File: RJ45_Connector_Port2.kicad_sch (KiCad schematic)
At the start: 8 parts, among them J1 0826-1X4T-43-F

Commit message: Adding page title, and confidential for now
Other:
- title: (none) -> RJ45 Connector Port 2
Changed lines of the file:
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@@
 	(paper "A4")
 	(title_block
+		(title "RJ45 Connector Port 2")
 		(date "2025-12-21")
 		(rev "Rev. A")
 		(company "Kebag-Logic <contact@kebag-logic.com>")
+		(comment 1 "Confidential")
 	)
 	(junction

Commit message: fixes ERC errors in DC/DC converters
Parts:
- C11, C12, C13, C14: footprint Capacitor_SMD:C_0201_0603Metric -> KL_Footprints:C_0603; Dielectric X7R -> (none); Farnell 4539043 -> (none); Package_in_inch 0603 -> (none); Tolerance_in_pct 10 -> (none)
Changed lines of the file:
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@@
 		(dnp no)
 		(property "Reference" "C13"
-			(at 80.01 58.674 90)
-			(effects
-				(font
-					(size 1.27 1.27)
-				)
+			(at 77.47 61.595 0)
+			(effects
+				(font
+					(size 1.27 1.27)
+				)
+				(justify left)
 			)
 		)
 		(property "Value" "100n"
-			(at 80.01 65.532 90)
-			(effects
-				(font
-					(size 1.27 1.27)
-				)
-			)
-		)
-		(property "Footprint" "Capacitor_SMD:C_0201_0603Metric"
+			(at 82.55 61.595 0)
+			(effects
+				(font
+					(size 1.27 1.27)
+				)
+				(justify left)
+			)
+		)
+		(property "Footprint" "KL_Footprints:C_0603"
 			(at 83.82 61.2648 0)
 			(effects
@@
 		)
 		(property "LCSC" "C1591"
-			(at 80.01 62.23 0)
-			(effects
-				(font
-					(size 1.27 1.27)
-				)
-				(hide yes)
-			)
-		)
-		(property "Tolerance_in_pct" "10"
-			(at 80.01 62.23 0)
-			(effects
-				(font
-					(size 1.27 1.27)
-				)
-				(hide yes)
-			)
-		)
-		(property "Dielectric" "X7R"
-			(at 80.01 62.23 0)
-			(effects
-				(font
-					(size 1.27 1.27)
-				)
-				(hide yes)
-			)
-		)
-		(property "Package_in_inch" "0603"
-			(at 80.01 62.23 0)
-			(effects
-				(font
-					(size 1.27 1.27)
-				)
-				(hide yes)
-			)
-		)
-		(property "Farnell" "4539043"
 			(at 80.01 62.23 0)
 			(effects
@@
 		(dnp no)
 		(property "Reference" "C11"
-			(at 80.01 38.354 90)
-			(effects
-				(font
-					(size 1.27 1.27)
-				)
+			(at 82.55 42.545 0)
+			(effects
+				(font
+					(size 1.27 1.27)
+				)
+				(justify left)
 			)
 		)
 		(property "Value" "100n"
-			(at 80.01 45.212 90)
-			(effects
-				(font
-					(size 1.27 1.27)
-				)
-			)
-		)
-		(property "Footprint" "Capacitor_SMD:C_0201_0603Metric"
+			(at 77.47 42.545 0)
+			(effects
+				(font
+					(size 1.27 1.27)
+				)
+				(justify left)
+			)
+		)
+		(property "Footprint" "KL_Footprints:C_0603"
 			(at 76.2 42.8752 0)
 			(effects
@@
 		)
 		(property "LCSC" "C1591"
-			(at 80.01 41.91 0)
-			(effects
-				(font
-					(size 1.27 1.27)
-				)
-				(hide yes)
-			)
-		)
-		(property "Tolerance_in_pct" "10"
-			(at 80.01 41.91 0)
-			(effects
-				(font
-					(size 1.27 1.27)
-				)
-				(hide yes)
-			)
-		)
-		(property "Dielectric" "X7R"
-			(at 80.01 41.91 0)
-			(effects
-				(font
-					(size 1.27 1.27)
-				)
-				(hide yes)
-			)
-		)
-		(property "Package_in_inch" "0603"
-			(at 80.01 41.91 0)
-			(effects
-				(font
-					(size 1.27 1.27)
-				)
-				(hide yes)
-			)
-		)
-		(property "Farnell" "4539043"
 			(at 80.01 41.91 0)
 			(effects
@@
 		(dnp no)
 		(property "Reference" "C12"
-			(at 80.01 48.768 90)
-			(effects
-				(font
-					(size 1.27 1.27)
-				)
+			(at 77.47 51.435 0)
+			(effects
+				(font
+					(size 1.27 1.27)
+				)
+				(justify left)
 			)
 		)
 		(property "Value" "100n"
-			(at 80.01 55.372 90)
-			(effects
-				(font
-					(size 1.27 1.27)
-				)
-			)
-		)
-		(property "Footprint" "Capacitor_SMD:C_0201_0603Metric"
+			(at 82.55 51.435 0)
+			(effects
+				(font
+					(size 1.27 1.27)
+				)
+				(justify left)
+			)
+		)
+		(property "Footprint" "KL_Footprints:C_0603"
 			(at 83.82 51.1048 0)
 			(effects
@@
 		)
 		(property "LCSC" "C1591"
-			(at 80.01 52.07 0)
-			(effects
-				(font
-					(size 1.27 1.27)
-				)
-				(hide yes)
-			)
-		)
-		(property "Tolerance_in_pct" "10"
-			(at 80.01 52.07 0)
-			(effects
-				(font
-					(size 1.27 1.27)
-				)
-				(hide yes)
-			)
-		)
-		(property "Dielectric" "X7R"
-			(at 80.01 52.07 0)
-			(effects
-				(font
-					(size 1.27 1.27)
-				)
-				(hide yes)
-			)
-		)
-		(property "Package_in_inch" "0603"
-			(at 80.01 52.07 0)
-			(effects
-				(font
-					(size 1.27 1.27)
-				)
-				(hide yes)
-			)
-		)
-		(property "Farnell" "4539043"
 			(at 80.01 52.07 0)
 			(effects
@@
 		(dnp no)
 		(property "Reference" "C14"
-			(at 80.01 68.834 90)
-			(effects
-				(font
-					(size 1.27 1.27)
-				)
+			(at 77.47 71.755 0)
+			(effects
+				(font
+					(size 1.27 1.27)
+				)
+				(justify left)
 			)
 		)
 		(property "Value" "100n"
-			(at 80.01 75.946 90)
-			(effects
-				(font
-					(size 1.27 1.27)
-				)
-			)
-		)
-		(property "Footprint" "Capacitor_SMD:C_0201_0603Metric"
+			(at 82.55 71.755 0)
+			(effects
+				(font
+					(size 1.27 1.27)
+				)
+				(justify left)
+			)
+		)
+		(property "Footprint" "KL_Footprints:C_0603"
 			(at 83.82 71.4248 0)
 			(effects
@@
 			(at 80.01 72.39 0)
 			(effects
-				(font
-					(size 1.27 1.27)
-				)
-				(hide yes)
-			)
-		)
-		(property "Tolerance_in_pct" "10"
-			(at 80.01 72.39 0)
-			(effects
-				(font
-					(size 1.27 1.27)
-				)
-				(hide yes)
-			)
-		)
-		(property "Dielectric" "X7R"
-			(at 80.01 72.39 0)
-			(effects
-				(font
-					(size 1.27 1.27)
-				)
-				(hide yes)
-			)
-		)
-		(property "Package_in_inch" "0603"
-			(at 80.01 72.39 0)
-			(effects
-				(font
-					(size 1.27 1.27)
-				)
-				(hide yes)
-			)
-		)
-		(property "Farnell" "4539043"
-			(at 80.01 72.39 0)
-			(effects

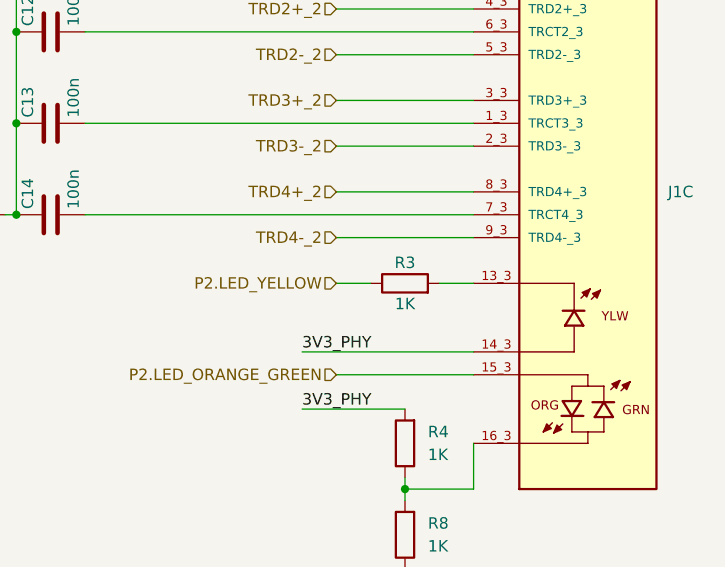
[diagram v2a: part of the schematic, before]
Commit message: updates components from my library misconfiguration. Refs: #1
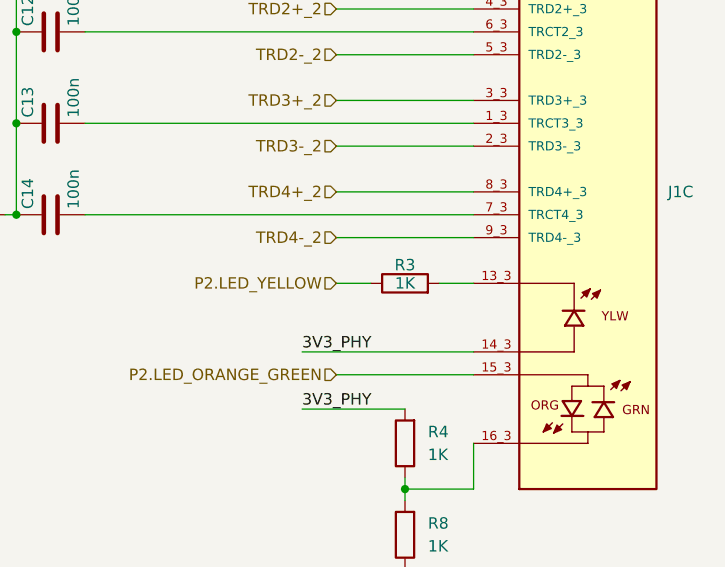
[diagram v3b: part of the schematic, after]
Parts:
- J1: footprint 0826-1X4T-43-F:BEL_0826-1X4T-43-F -> KL_Footprints:BEL_0826-1X4T-43-F
- R3, R4, R8: footprint KL_Footprints:C_0603 -> KL_Footprints:R_0603
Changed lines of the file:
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@@
 		(dnp no)
 		(property "Reference" "R3"
-			(at 119.38 77.724 90)
+			(at 119.38 77.978 90)
 			(effects
 				(font
@@
 		)
 		(property "Value" "1K"
-			(at 119.38 82.296 90)
-			(effects
-				(font
-					(size 1.27 1.27)
-				)
-			)
-		)
-		(property "Footprint" "KL_Footprints:C_0603"
+			(at 119.38 80.01 90)
+			(effects
+				(font
+					(size 1.27 1.27)
+				)
+			)
+		)
+		(property "Footprint" "KL_Footprints:R_0603"
 			(at 119.38 81.788 90)
 			(effects
@@
 			)
 		)
-		(property "Footprint" "KL_Footprints:C_0603"
+		(property "Footprint" "KL_Footprints:R_0603"
 			(at 121.158 97.79 90)
 			(effects
@@
 			)
 		)
-		(property "Footprint" "0826-1X4T-43-F:BEL_0826-1X4T-43-F"
+		(property "Footprint" "KL_Footprints:BEL_0826-1X4T-43-F"
 			(at 139.7 69.85 0)
 			(effects
@@
 			)
 		)
-		(property "Footprint" "KL_Footprints:C_0603"
+		(property "Footprint" "KL_Footprints:R_0603"
 			(at 121.158 107.95 90)
 			(effects

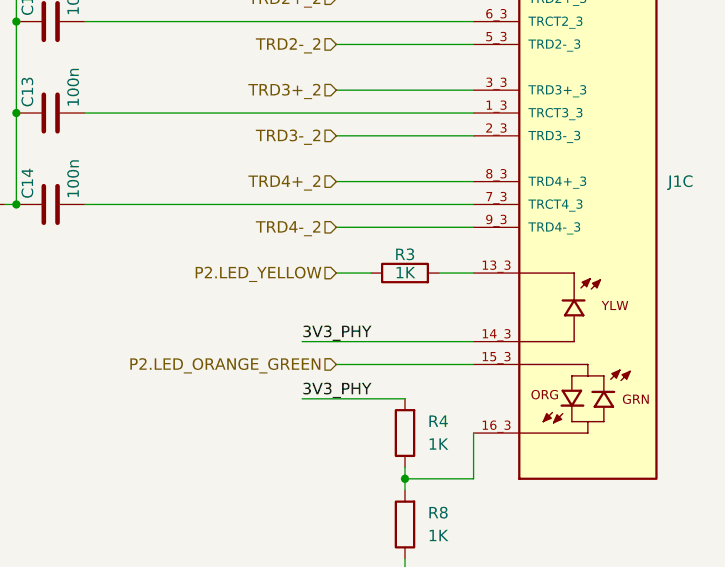
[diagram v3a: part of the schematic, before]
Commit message: removes unused busses, adds cheaper 0R resistor, clean up to fix ERC errors. Refs: #1
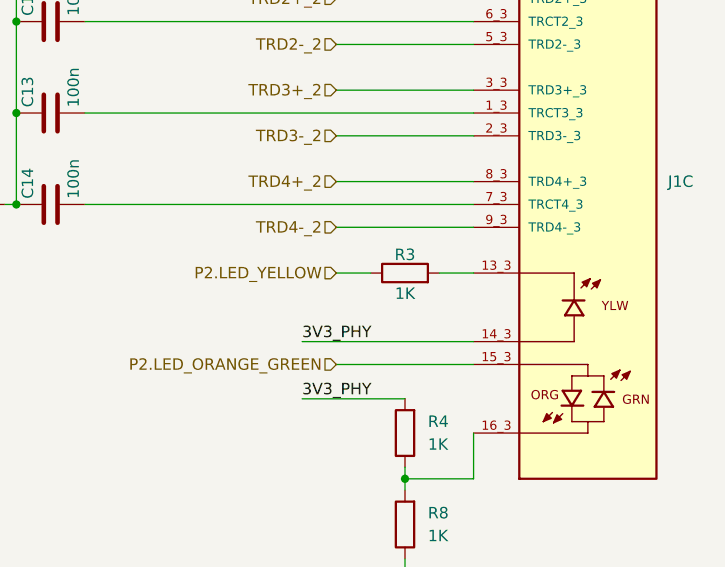
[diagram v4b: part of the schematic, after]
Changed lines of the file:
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@@
 		)
 		(property "Value" "1K"
-			(at 119.38 80.01 90)
+			(at 119.38 82.296 90)
 			(effects
 				(font
